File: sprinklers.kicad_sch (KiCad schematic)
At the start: 37 parts, among them J2 Conn_Coaxial_Power, K1 SANYOU_SRD_Form_C, K2 SANYOU_SRD_Form_C, K3 SANYOU_SRD_Form_C, K4 SANYOU_SRD_Form_C, K5 SANYOU_SRD_Form_C, K6 SANYOU_SRD_Form_C, Q1 Q_NMOS_GDS, Q2 Q_NMOS_GDS, Q3 Q_NMOS_GDS, Q4 Q_NMOS_GDS, Q5 Q_NMOS_GDS, Q6 Q_NMOS_GDS, U1 LM2596S-5, U2 ESP32-WROOM-32D, U3 AP1117-33

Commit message: orgenize schematic
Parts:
- D1: LCSC C2297 -> C84256
- D3: LCSC C84256 -> C2297
- D5: LCSC (none) -> C968568
- R4: LCSC C4410 -> C17451
- R8: LCSC C17451 -> C4410
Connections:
- net AC: no longer names the net of K1.1, K2.1, K3.1, K4.1, K5.1, K6.1
- net AC: no longer C5.1, D4.1 (K), D4.2 (A), J2.1 (In), U1.1 (VIN)
- new net: C5.1, D4.1 (K), U1.1 (VIN)
- new net: D4.2 (A), J2.1 (In)
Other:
- note added: "AC24V --> DC5V"
- note added: "DC5V --> DC3V3"
- moved on the sheet: C5, C6, D4, D5, J2, L1, U1

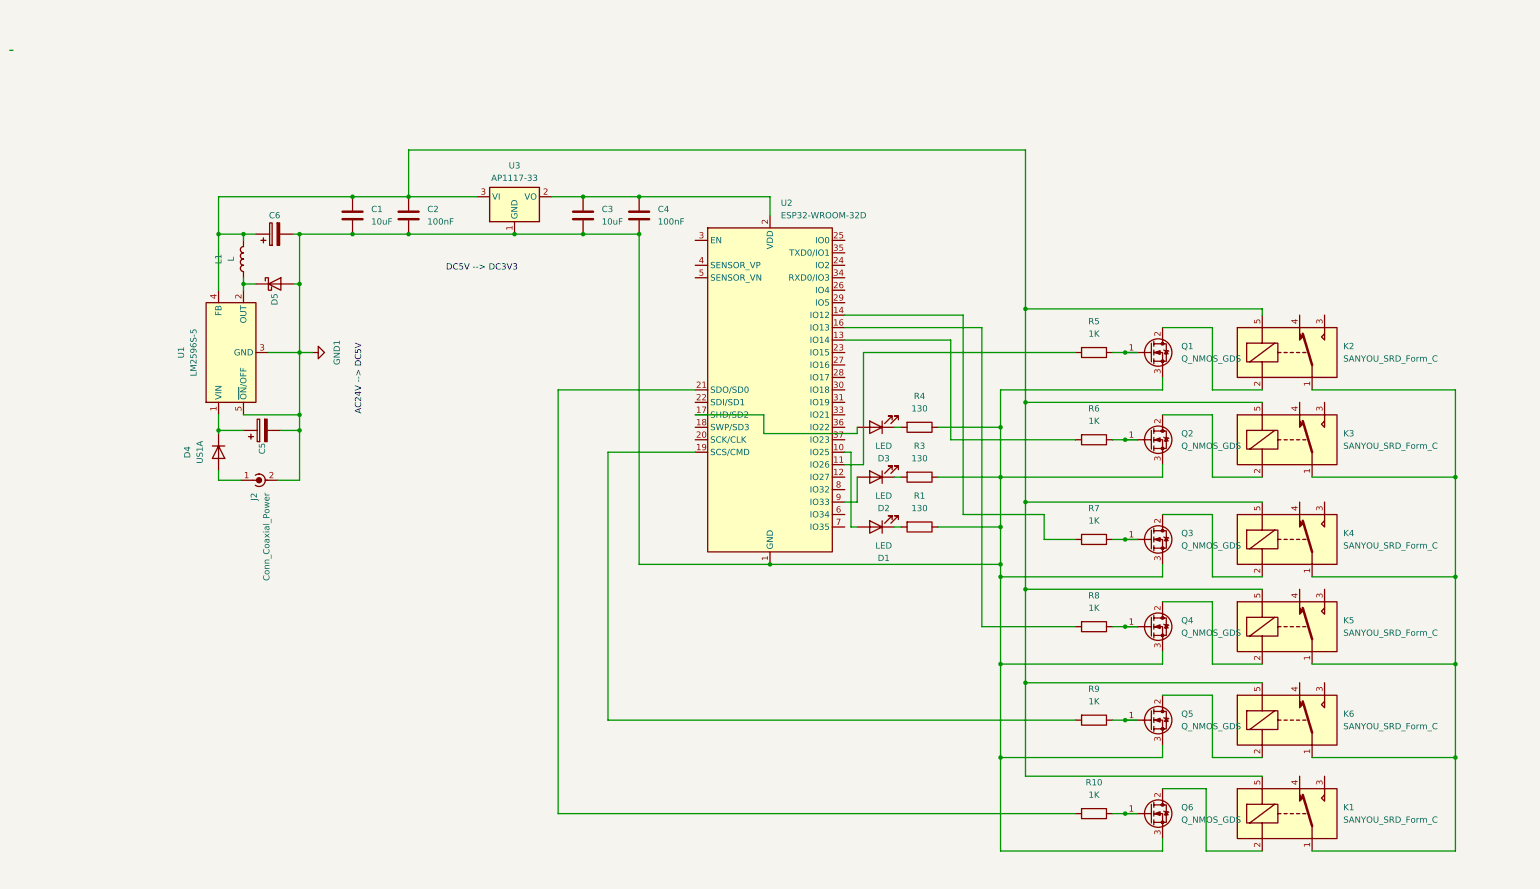
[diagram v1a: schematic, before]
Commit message: Replacing inductor
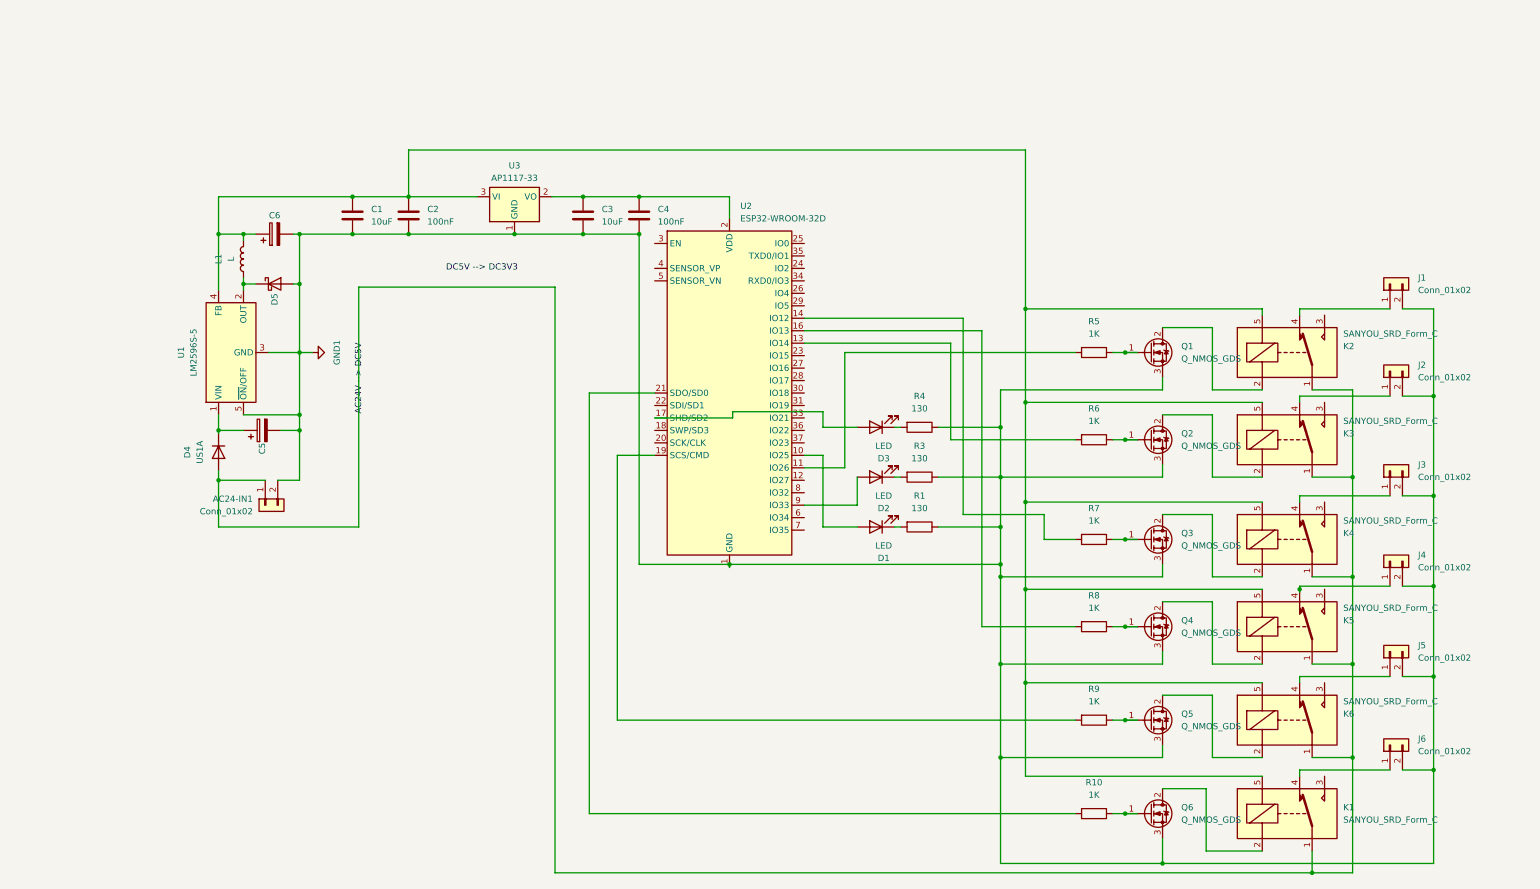
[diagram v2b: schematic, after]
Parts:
- removed J2: Conn_Coaxial_Power, Connector_BarrelJack:BarrelJack_GCT_DCJ200-10-A_Horizontal, symbol Connector:Conn_Coaxial_Power
- added AC24-IN1, J1, J2, J3, J4, J5, J6: Conn_01x02, Connector:JWT_A3963_1x02_P3.96mm_Vertical, symbol Connector_Generic:Conn_01x02
- D1: LCSC C84256 -> C2297
- D3: LCSC C2297 -> C84256
- L1: footprint Inductor_SMD:L_1008_2520Metric -> Inductor_SMD:L_12x12mm_H8mm; LCSC (none) -> C2983075
- R4: LCSC C17451 -> C4410
- R9: LCSC C4410 -> C17451
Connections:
- net GND1: now also AC24-IN1.2 (Pin_2), J1.2 (Pin_2), J2.2 (Pin_2), J3.2 (Pin_2), J4.2 (Pin_2), J5.2 (Pin_2), J6.2 (Pin_2)
- net at K1.1, K2.1, K3.1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: now also D4.2 (A), AC24-IN1.1 (Pin_1)
- net at K1.4: now also J6.1 (Pin_1)
- net at K4.4: now also J3.1 (Pin_1)
- net at K5.4: now also J4.1 (Pin_1)
- net at K2.4: now also J1.1 (Pin_1)
- net at K6.4: now also J5.1 (Pin_1)
- net at K3.4: now also J2.1 (Pin_1)
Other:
- moved on the sheet: U2

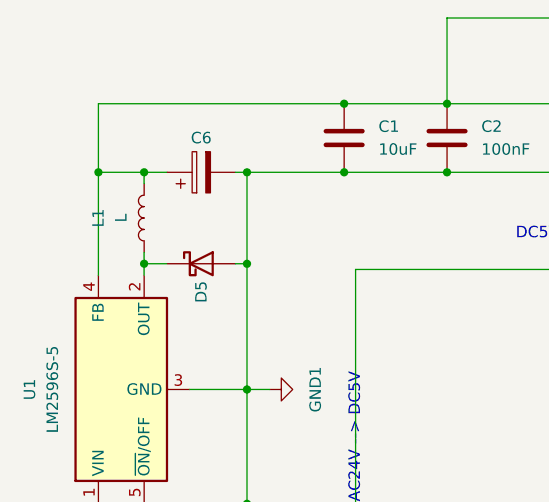
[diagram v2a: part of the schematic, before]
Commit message: tx/rx fix
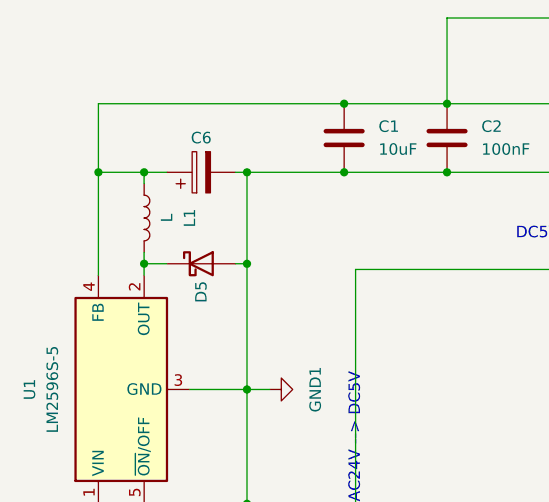
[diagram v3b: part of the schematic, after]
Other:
- moved on the sheet: L1
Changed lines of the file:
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@@
     )
   )
-  (symbol (lib_id "Device:L") (at 28.575 38.1 180) (unit 1)
-    (in_bom yes) (on_board yes) (dnp no) (fields_autoplaced)
-    (property "Reference" "L1" (at 23.495 38.1 90)
+  (symbol (lib_id "Device:L") (at 28.575 38.1 0) (mirror x) (unit 1)
+    (in_bom yes) (on_board yes) (dnp no)
+    (property "Reference" "L1" (at 33.655 38.1 90)
       (effects (font (size 1.27 1.27)))
     )
-    (property "Value" "L" (at 26.035 38.1 90)
+    (property "Value" "L" (at 31.115 38.1 90)
       (effects (font (size 1.27 1.27)))
     )
@@
       (effects (font (size 1.27 1.27)) hide)
     )
-    (property "LCSC" "C2983075" (at 23.495 38.1 0)
+    (property "LCSC" "C2983075" (at 33.655 38.1 0)
       (effects (font (size 1.27 1.27)) hide)
     )

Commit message: V1.1.0 with notation
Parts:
- added D6, D7, D8: 900mV@2A 30ns 2A 50V DO-214AA Diodes, Diode_SMD:D_SMB, symbol Diode:US1A
- added RV1: R_Potentiometer_Small, Potentiometer_THT:Potentiometer_Bourns_3296Y_Vertical, symbol Device:R_Potentiometer_Small
- added SENSOR1: Conn_01x02, Connector:JWT_A3963_1x02_P3.96mm_Vertical, symbol Connector_Generic:Conn_01x02
- AC24-IN1, J1, J2, J3, J4, J5, J6: LCSC C474894 -> C3031444
- C1: footprint Capacitor_SMD:C_0402_1005Metric -> Capacitor_SMD:C_0805_2012Metric
- C2, C4: footprint Capacitor_SMD:C_0402_1005Metric -> Capacitor_SMD:C_0603_1608Metric
- C3: footprint Capacitor_SMD:C_0402_1005Metric -> Capacitor_SMD:C_0805_2012Metric; LCSC C13585 -> C440198
- D1: LCSC C2297 -> C84256
- D2: LCSC C2296 -> C2297
- D3: LCSC C84256 -> C2296
- D4: value US1A -> 900mV@2A 30ns 2A 50V DO-214AA Diodes; footprint Diode_SMD:D_SMA -> Diode_SMD:D_SMB; LCSC C183422 -> C5224093
- Q1, Q2, Q3, Q4, Q5, Q6: LCSC C98152 -> C122491
- R9: LCSC C17451 -> C4410
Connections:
- net GND1: now also D6.2 (A), D8.2 (A), RV1.1; no longer AC24-IN1.2 (Pin_2)
- net at AC24-IN1.1 (Pin_1), D4.2 (A), K1.1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: now also D6.1 (K)
- net at C3.1, C4.1, U2.2 (VDD)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: now also SENSOR1.2 (Pin_2)
- net at C5.1, D4.1 (K), U1.1 (VIN): now also D7.1 (K)
- net at U2.9 (IO33): now also RV1.2, SENSOR1.1 (Pin_1); no longer D2.2 (A)
- net at U2.8 (IO32): now also D2.2 (A)
- new net: AC24-IN1.2 (Pin_2), D7.2 (A), D8.1 (K)
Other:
- moved on the sheet: AC24-IN1, D4

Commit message: applying fixed after review
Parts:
- removed R3, R4: 130, Resistor_SMD:R_1206_3216Metric, symbol Device:R
- removed R6: 1K, Resistor_SMD:R_1206_3216Metric, symbol Device:R
- added C1 (x2): 25V 1uF X5R ±10% 0402 Multilayer Ceramic Capacito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, Capacitor_SMD:C_01005_0402Metric, symbol Device:C
- added D10, D11, D12, D13, D14, D9: 75V 400mW Single 1V@50mA 4ns 150mA SOD-123 Switch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, Diode_SMD:D_SOD-123, symbol Diode:US1A
- added EXT1, J8: Conn_01x04_Pin, Connector_PinHeader_2.54mm:PinHeader_1x04_P2.54mm_Vertical, symbol Connector:Conn_01x04_Pin
- added J11: Conn_01x02_Pin, Connector_PinHeader_2.54mm:PinHeader_1x02_P2.54mm_Vertical, symbol Connector:Conn_01x02_Pin
- added J9: Conn_01x03_Pin, Connector_PinHeader_2.54mm:PinHeader_1x03_P2.54mm_Vertical, symbol Connector:Conn_01x03_Pin
- added PROG/EXT1: Conn_01x06_Pin, Connector_PinHeader_2.54mm:PinHeader_1x06_P2.54mm_Vertical, symbol Connector:Conn_01x06_Pin
- added R1 (x5): 130, Resistor_SMD:R_0201_0603Metric, symbol Device:R
- added R6: 10K, Resistor_SMD:R_1206_3216Metric, symbol Device:R
- added R6: 1K, Resistor_SMD:R_1206_3216Metric, symbol Device:R
- added SW1: SW_SPST, Button_Switch_SMD:SW_SPST_TL3342, symbol Switch:SW_SPST
- C5, C6: footprint Capacitor_THT:CP_Radial_D8.0mm_P3.50mm -> Capacitor_THT:CP_Radial_D10.0mm_P5.00mm; LCSC C225865 -> C461457
- D1: LCSC C84256 -> C130721
- D2: LCSC C2297 -> C130719
- D3: LCSC C2296 -> C130724
- K1, K2, K3, K4, K5, K6: LCSC C24585 -> C35449
- L1: LCSC C2983075 -> C339951
- Q1, Q2, Q3, Q4, Q5, Q6: LCSC C122491 -> C3010
- R1: footprint Resistor_SMD:R_1206_3216Metric -> Resistor_SMD:R_0201_0603Metric; LCSC C4410 -> C22797
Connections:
- net GND1: now also R10.2, R5.2, R7.2, R8.2, R9.2, C1.1, C1.1, J11.2 (Pin_2), J8.4 (Pin_4), J9.3 (Pin_3), PROG/EXT1.2 (Pin_2), R1.1, R1.1, R6.2, SW1.2 (B); no longer J1.2 (Pin_2), J2.2 (Pin_2), J3.2 (Pin_2), J4.2 (Pin_2), J5.2 (Pin_2), J6.2 (Pin_2)
- net at J3.1 (Pin_1): now also K4.3; no longer K4.4
- net at K1.2: now also D14.1 (K); no longer Q6.2 (D)
- net at K1.3: now also J6.1 (Pin_1)
- net at K1.4: no longer J6.1 (Pin_1)
- net 5V: now reaches C1.1, C2.1, C6.1, K1.5, K2.5, K3.5, K4.5, K5.5, K6.5, L1.2, U1.4 (FB), U3.3 (VI)
- net 5V: now also J9.1 (Pin_1)
- net at Q1.1 (G), R5.1: now also U2.33 (IO21)
- net at U2.11 (IO26): now also Q3.1 (G), R7.1; no longer R5.2
- net at J5.1 (Pin_1): now also K6.3; no longer K6.4
- net at D1.2 (A): now also U2.28 (IO17); no longer U2.10 (IO25)
- net at U2.14 (IO12): now also Q6.1 (G), R10.1; no longer R7.2
- net at J1.1 (Pin_1): now also K2.3; no longer K2.4
- net at K2.2: now also D11.1 (K); no longer Q1.2 (D)
- net at Q4.1 (G), R8.1: now also U2.12 (IO27)
- net at K5.2: now also D12.1 (K); no longer Q4.2 (D)
- net at C5.1, D4.1 (K), D7.1 (K)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: now also C1.2
- net at AC24-IN1.2 (Pin_2), D7.2 (A), D8.1 (K): now also J1.2 (Pin_2), J2.2 (Pin_2), J3.2 (Pin_2), J4.2 (Pin_2), J5.2 (Pin_2), J6.2 (Pin_2)
- net at D5.1 (K), L1.1, U1.2 (OUT): now also C1.2
- net at Q2.1 (G): now also U2.10 (IO25), R6.1
- net at Q2.2 (D): now also D10.2 (A); no longer K3.2
- net at U2.21 (SDO/SD0): no longer R10.2
- net at RV1.2, SENSOR1.1 (Pin_1): now also U2.6 (IO34); no longer U2.9 (IO33)
- net 3V3: now reaches C3.1, C4.1, SENSOR1.2 (Pin_2), U2.2 (VDD), U3.2 (VO)
- net 3V3: now also J9.2 (Pin_2), PROG/EXT1.1 (Pin_1), R6.1
- net at K4.2: now also D9.1 (K); no longer Q3.2 (D)
- net at K5.3: now also J4.1 (Pin_1)
- net at K5.4: no longer J4.1 (Pin_1)
- net at D3.1 (K): now also R1.2
- net at D2.1 (K): now also R1.2
- net at D3.2 (A): now also U2.23 (IO15); no longer U2.17 (SHD/SD2)
- net at K6.2: now also D13.1 (K); no longer Q5.2 (D)
- net at J2.1 (Pin_1): now also K3.3; no longer K3.4
- net at Q5.1 (G), R9.1: now also U2.13 (IO14)
- net at U2.19 (SCS/CMD): no longer R9.2
- net at U2.8 (IO32): now also EXT1.2 (Pin_2); no longer D2.2 (A)
- net at U2.16 (IO13): now also R1.2; no longer R8.2
- net at U2.25 (IO0): now also PROG/EXT1.3 (Pin_3)
- net at U2.26 (IO4): now also R1.2
- net at U2.27 (IO16): now also D2.2 (A)
- net at U2.29 (IO5): now also R1.2
- net at U2.3 (EN): now also J11.1 (Pin_1), PROG/EXT1.6 (Pin_6), R6.2, SW1.1 (A)
- net at U2.34 (RXD0/IO3): now also PROG/EXT1.4 (Pin_4)
- net at U2.35 (TXD0/IO1): now also PROG/EXT1.5 (Pin_5)
- net at U2.36 (IO22): now also EXT1.3 (Pin_3)
- net at U2.37 (IO23): now also EXT1.4 (Pin_4)
- net at U2.7 (IO35): now also EXT1.1 (Pin_1)
- new net: D11.2 (A), Q1.2 (D)
- new net: J8.2 (Pin_2), R1.1
- new net: D13.2 (A), Q5.2 (D)
- new net: D12.2 (A), Q4.2 (D)
- new net: J8.1 (Pin_1), R1.1
- new net: D14.2 (A), Q6.2 (D)
- new net: D10.1 (K), K3.2
- new net: D9.2 (A), Q3.2 (D)
- new net: J8.3 (Pin_3), R1.1
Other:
- moved on the sheet: AC24-IN1, C5, D1, D2, D3, D4, D6, D7, D8, R1, U1, U2

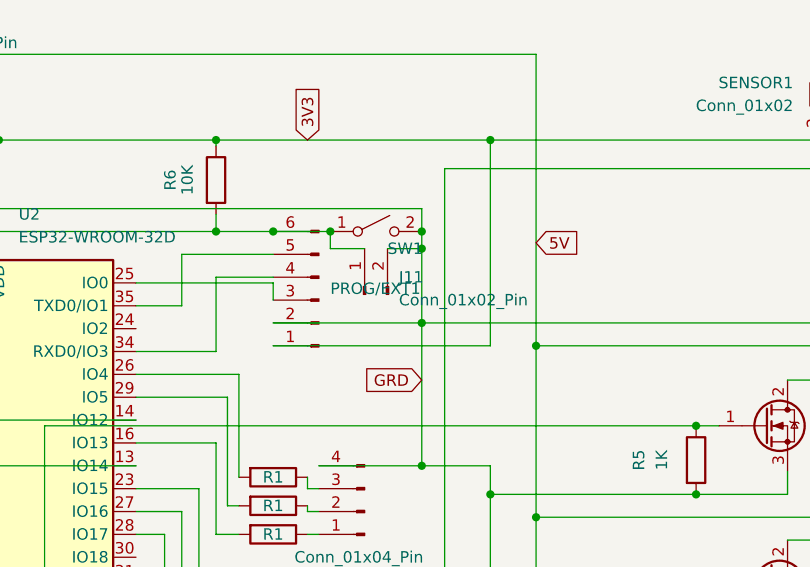
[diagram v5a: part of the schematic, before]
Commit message: fix capacitor and connect q3
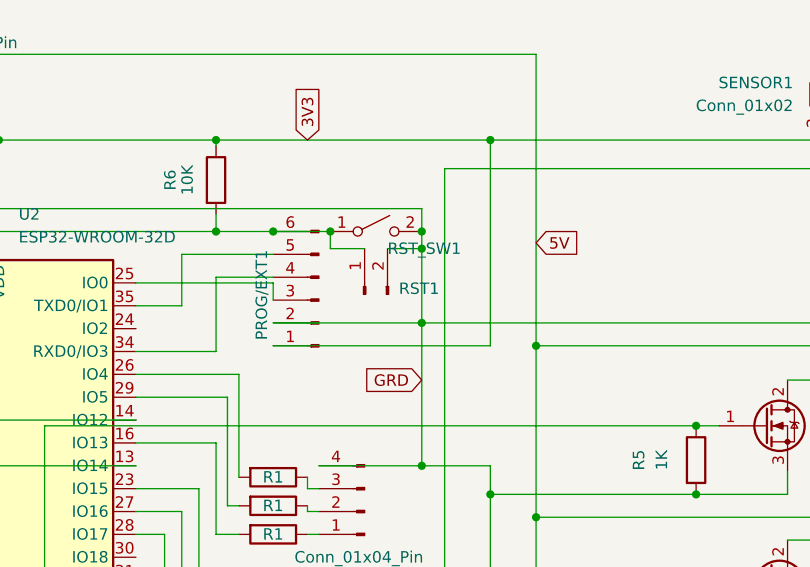
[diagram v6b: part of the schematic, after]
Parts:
- C1: footprint Capacitor_SMD:C_01005_0402Metric -> Capacitor_SMD:C_0402_1005Metric
- R1: LCSC C22797 -> C22808
- renumbered J11 to RST1, SW1 to RST_SW1
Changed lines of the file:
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@@
       (effects (font (size 1.27 1.27)) hide)
     )
-    (property "LCSC" "C22797" (at 167.005 82.55 0)
+    (property "LCSC" "C22808" (at 167.005 82.55 0)
       (effects (font (size 1.27 1.27)) hide)
     )
@@
   (symbol (lib_id "Switch:SW_SPST") (at 170.18 35.56 0) (unit 1)
     (in_bom yes) (on_board yes) (dnp no)
-    (property "Reference" "SW1" (at 171.45 37.465 0)
+    (property "Reference" "RST_SW1" (at 171.45 37.465 0)
       (effects (font (size 1.27 1.27)) (justify left))
     )
@@
       (project "sprinklers"
         (path "/abcf66e9-3103-4da4-9926-73a03f14d5d3"
-          (reference "SW1") (unit 1)
+          (reference "RST_SW1") (unit 1)
         )
       )
@@
       (effects (font (size 1.27 1.27)) hide)
     )
-    (property "LCSC" "C22797" (at 158.75 59.69 0)
+    (property "LCSC" "C22808" (at 158.75 59.69 0)
       (effects (font (size 1.27 1.27)) hide)
     )
@@
   (symbol (lib_id "Connector:Conn_01x02_Pin") (at 168.91 42.545 90) (unit 1)
     (in_bom yes) (on_board yes) (dnp no) (fields_autoplaced)
-    (property "Reference" "J11" (at 172.72 40.64 90)
+    (property "Reference" "RST1" (at 172.72 41.91 90)
       (effects (font (size 1.27 1.27)) (justify right))
     )
     (property "Value" "Conn_01x02_Pin" (at 172.72 43.18 90)
-      (effects (font (size 1.27 1.27)) (justify right))
+      (effects (font (size 1.27 1.27)) (justify right) hide)
     )
     (property "Footprint" "Connector_PinHeader_2.54mm:PinHeader_1x02_P2.54mm_Vertical" (at 168.91 42.545 0)
@@
       (project "sprinklers"
         (path "/abcf66e9-3103-4da4-9926-73a03f14d5d3"
-          (reference "J11") (unit 1)
+          (reference "RST1") (unit 1)
         )
       )
@@
       (effects (font (size 1.27 1.27)) hide)
     )
-    (property "LCSC" "C22797" (at 167.005 71.12 0)
+    (property "LCSC" "C22808" (at 167.005 71.12 0)
       (effects (font (size 1.27 1.27)) hide)
     )
@@
       (effects (font (size 1.27 1.27)) hide)
     )
-    (property "LCSC" "C22797" (at 158.75 62.865 0)
+    (property "LCSC" "C22808" (at 158.75 62.865 0)
       (effects (font (size 1.27 1.27)) hide)
     )
@@
   )
   (symbol (lib_id "Connector:Conn_01x06_Pin") (at 163.83 43.18 180) (unit 1)
-    (in_bom yes) (on_board yes) (dnp no) (fields_autoplaced)
-    (property "Reference" "PROG/EXT1" (at 165.1 41.91 0)
+    (in_bom yes) (on_board yes) (dnp no)
+    (property "Reference" "PROG/EXT1" (at 157.48 47.625 90)
       (effects (font (size 1.27 1.27)) (justify right))
     )
@@
       (effects (font (size 1.27 1.27)) (justify left) hide)
     )
-    (property "Footprint" "Capacitor_SMD:C_01005_0402Metric" (at 30.48 53.0352 0)
+    (property "Footprint" "Capacitor_SMD:C_0402_1005Metric" (at 30.48 53.0352 0)
       (effects (font (size 1.27 1.27)) hide)
     )
@@
       (effects (font (size 1.27 1.27)) hide)
     )
-    (property "LCSC" "C22797" (at 167.005 76.835 0)
+    (property "LCSC" "C22808" (at 167.005 76.835 0)
       (effects (font (size 1.27 1.27)) hide)
     )
@@
       (effects (font (size 1.27 1.27)) (justify left) hide)
     )
-    (property "Footprint" "Capacitor_SMD:C_01005_0402Metric" (at 27.94 85.4202 0)
+    (property "Footprint" "Capacitor_SMD:C_0402_1005Metric" (at 27.94 85.4202 0)
       (effects (font (size 1.27 1.27)) hide)
     )
@@
       (effects (font (size 1.27 1.27)) hide)
     )
-    (property "LCSC" "C22797" (at 158.75 56.515 0)
-      (effects (font (size 1.27 1.27)) hide)
-    )
+    (property "LCSC" "C22808" (at 158.75 56.515 0)
+      (effects (font (size 1.27 1.27)) hide)
+    )
